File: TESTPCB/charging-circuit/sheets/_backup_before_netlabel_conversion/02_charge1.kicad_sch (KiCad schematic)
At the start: 19 parts, among them U10 BQ25606RGER, U22 SRP4020TA-1R0M

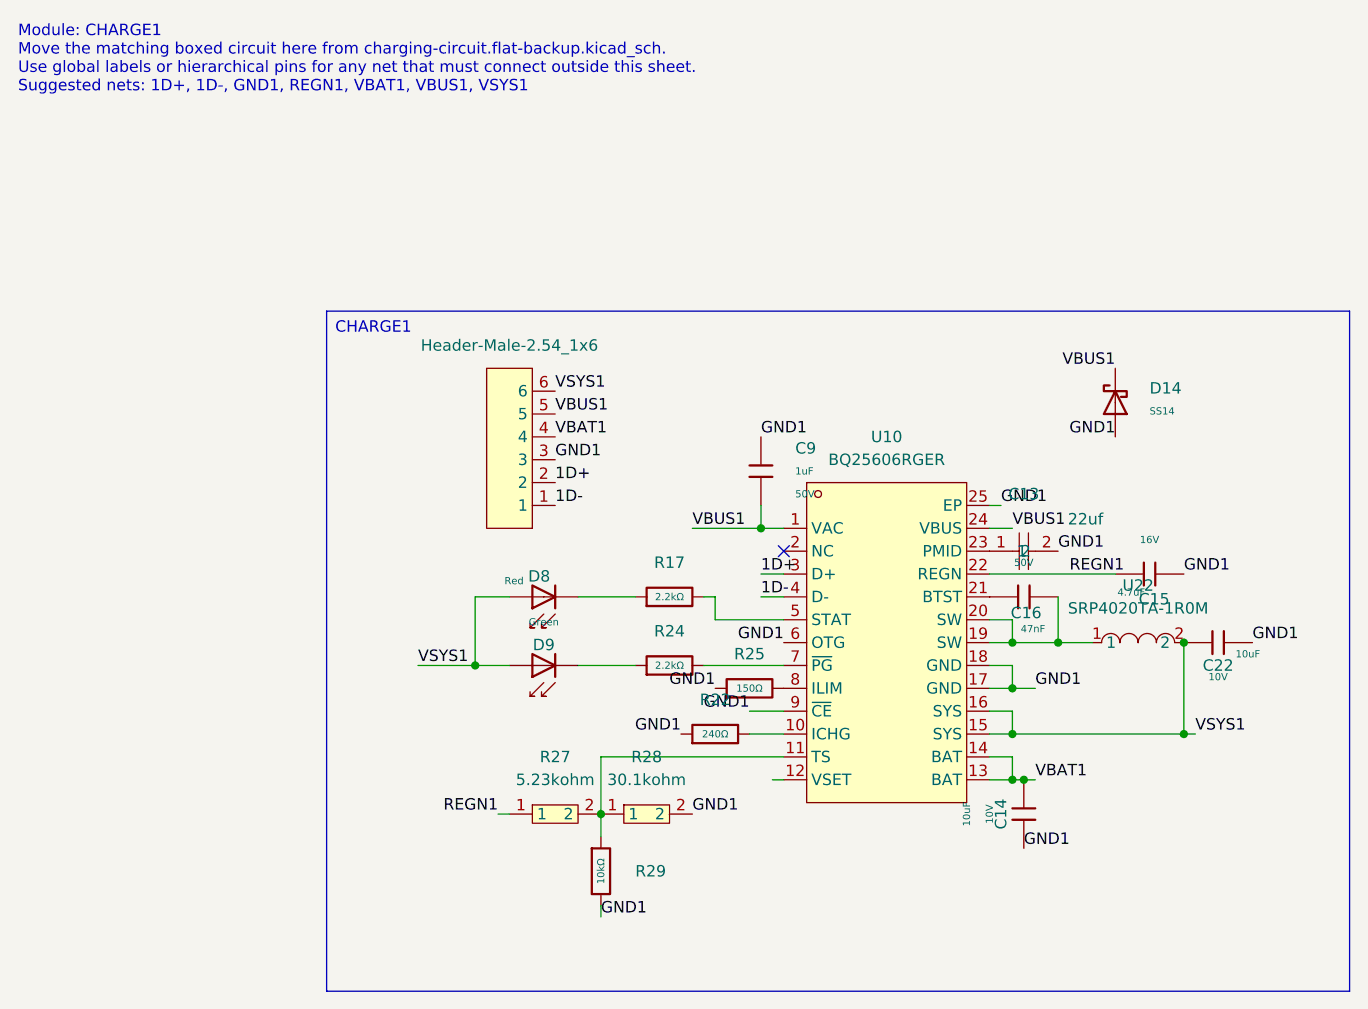
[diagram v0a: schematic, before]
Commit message: Fixed formatting issues, now the hierachal sheets are all labeled as net labels and when we want to expose their pins we will make them into hierchal or global pins
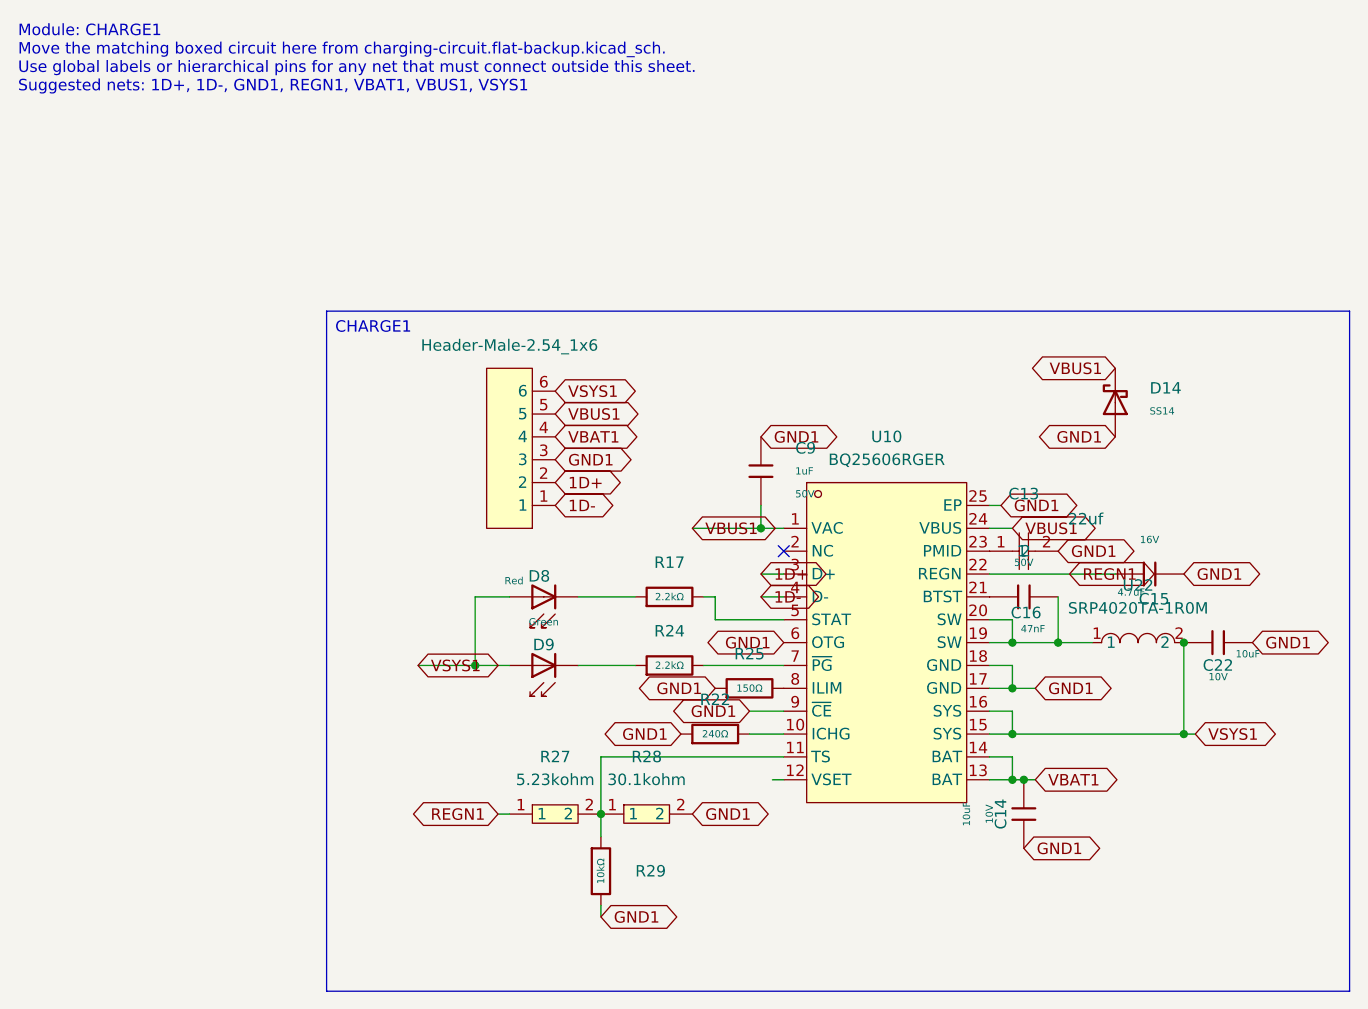
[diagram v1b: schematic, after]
